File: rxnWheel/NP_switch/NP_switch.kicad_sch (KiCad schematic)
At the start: 10 parts, among them Q3 Si4162DY

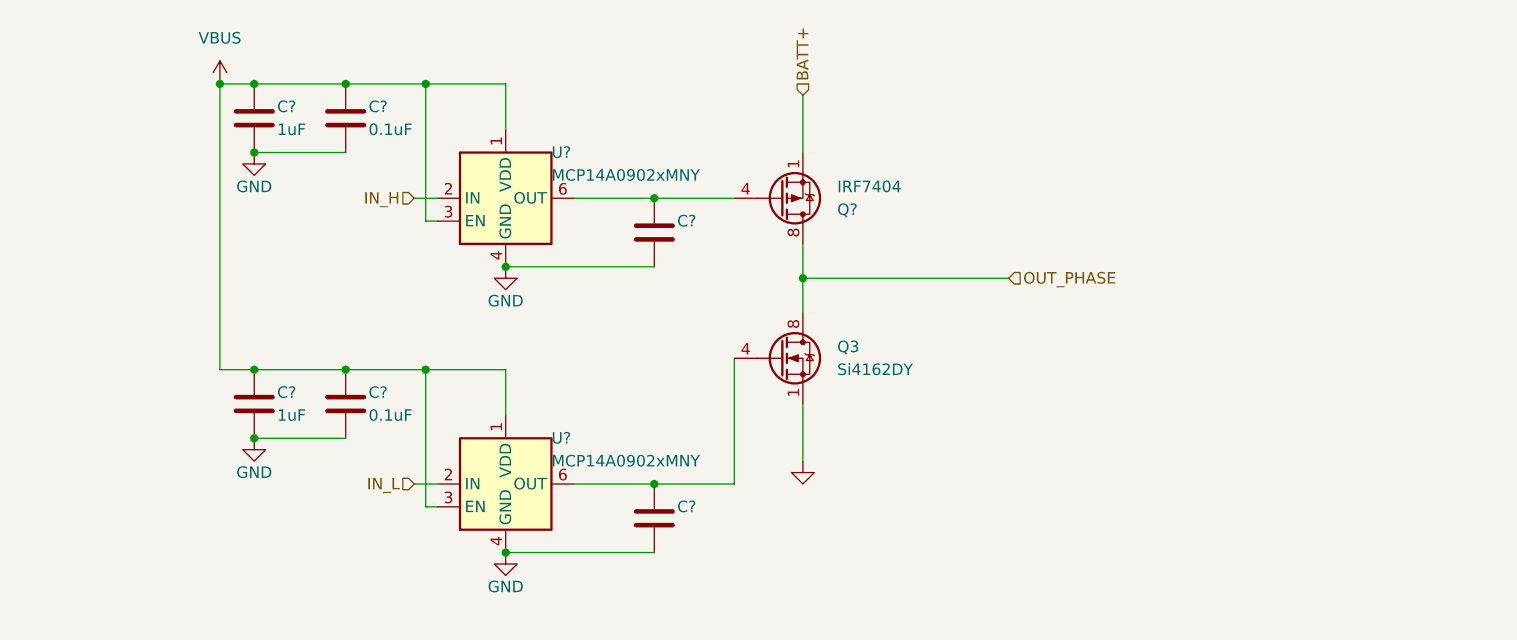
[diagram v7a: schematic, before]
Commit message: Cap
Caps vbus --> gnd
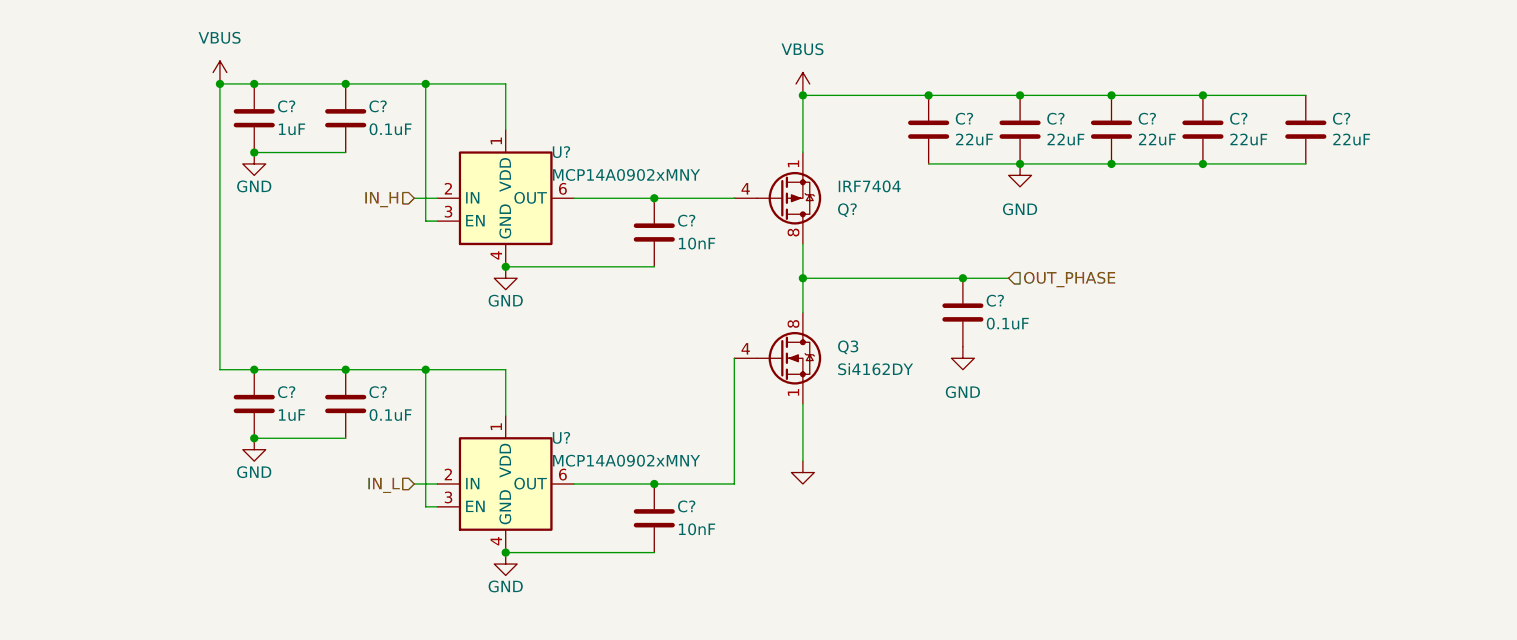
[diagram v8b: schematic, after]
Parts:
- added C?: 0.1uF, Capacitor_SMD:C_0805_2012Metric, symbol Device:C
- added C? (x5): 22uF, Capacitor_SMD:C_1210_3225Metric, symbol Device:C
- C?: value (none) -> 10nF; footprint (none) -> Capacitor_SMD:C_0805_2012Metric
- C?: value (none) -> 10nF
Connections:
- net BATT+ is gone; now on net VBUS: Q?.1 (S), Q?.2 (S), Q?.3 (S)
- net GND: now also C?.2, C?.2, C?.2, C?.2, C?.2, C?.2
- net OUT_PHASE: now also C?.1
- net VBUS: now also C?.1, C?.1, C?.1, C?.1, C?.1
